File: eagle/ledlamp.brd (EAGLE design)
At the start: 64.4 x 57.1 mm, 22 parts

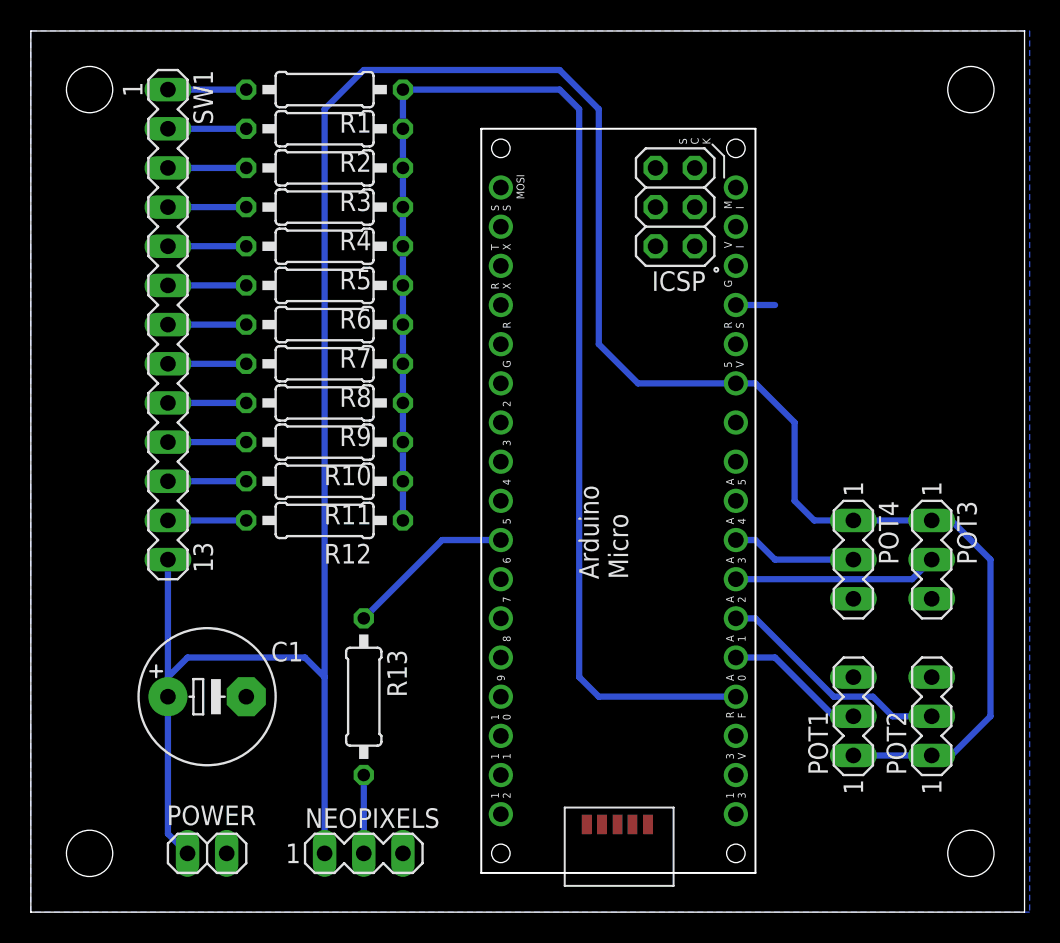
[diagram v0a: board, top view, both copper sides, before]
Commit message: Add pull-down resistor as voltage divider for A0
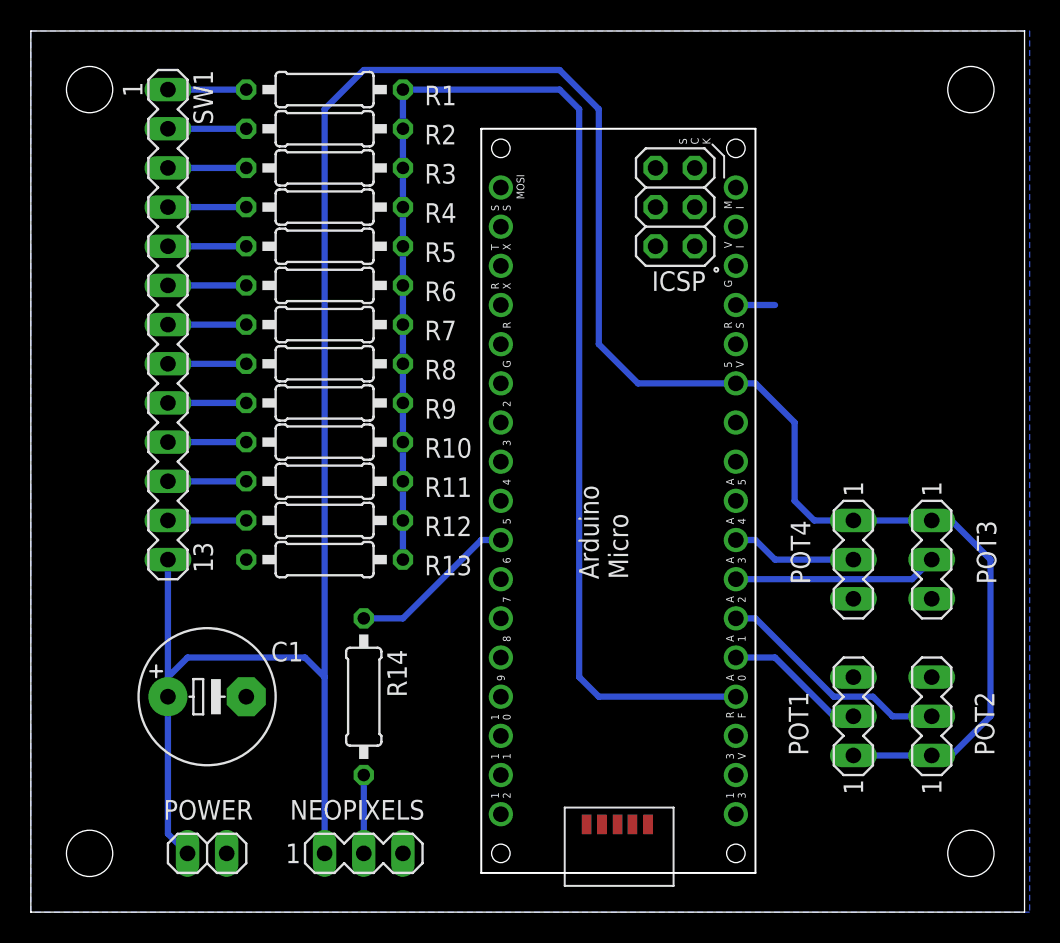
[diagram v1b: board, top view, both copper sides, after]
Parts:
- added R14: 380, rcl:0207/10
- R1: value (none) -> 330
- R10: value (none) -> 47k
- R11: value (none) -> 68k
- R12: value (none) -> 92k
- R13: value 380 -> 1k
- R2: value (none) -> 470
- R3: value (none) -> 680
- R4: value (none) -> 920
- R5: value (none) -> 3.3k
- R6: value (none) -> 4.7k
- R7: value (none) -> 6.8k
- R8: value (none) -> 9.2k
- R9: value (none) -> 33k
- moved R13 9.25 mm to (19.1, 22.9), turned to 0 degrees
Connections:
- net GND: now also R13.1
- net N$14: now also R13.2
- net N$22: now also R14.1; no longer R13.1
- net N$23: now also R14.2; no longer R13.2
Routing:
- net N$14: track 87.4 -> 90.0 mm
